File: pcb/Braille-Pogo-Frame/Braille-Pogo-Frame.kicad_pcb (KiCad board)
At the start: 2 copper layers, 99 x 95 mm, 64 parts, among them J1 Conn_01x06, J10 Screw_Terminal_01x02, J2 Conn_01x06, J3 Conn_01x06, J4 Conn_01x06, J9 Conn_01x02, M1 Stepper_Motor_bipolar, M2 Stepper_Motor_bipolar, M3 Stepper_Motor_bipolar, M4 Stepper_Motor_bipolar, SW1 SW_Push, SW2 SW_Push, U1 DRV8847SPWR, U2 DRV8847SPWR, U3 DRV8847SPWR, U4 DRV8847SPWR, U9 RP2040-Zero

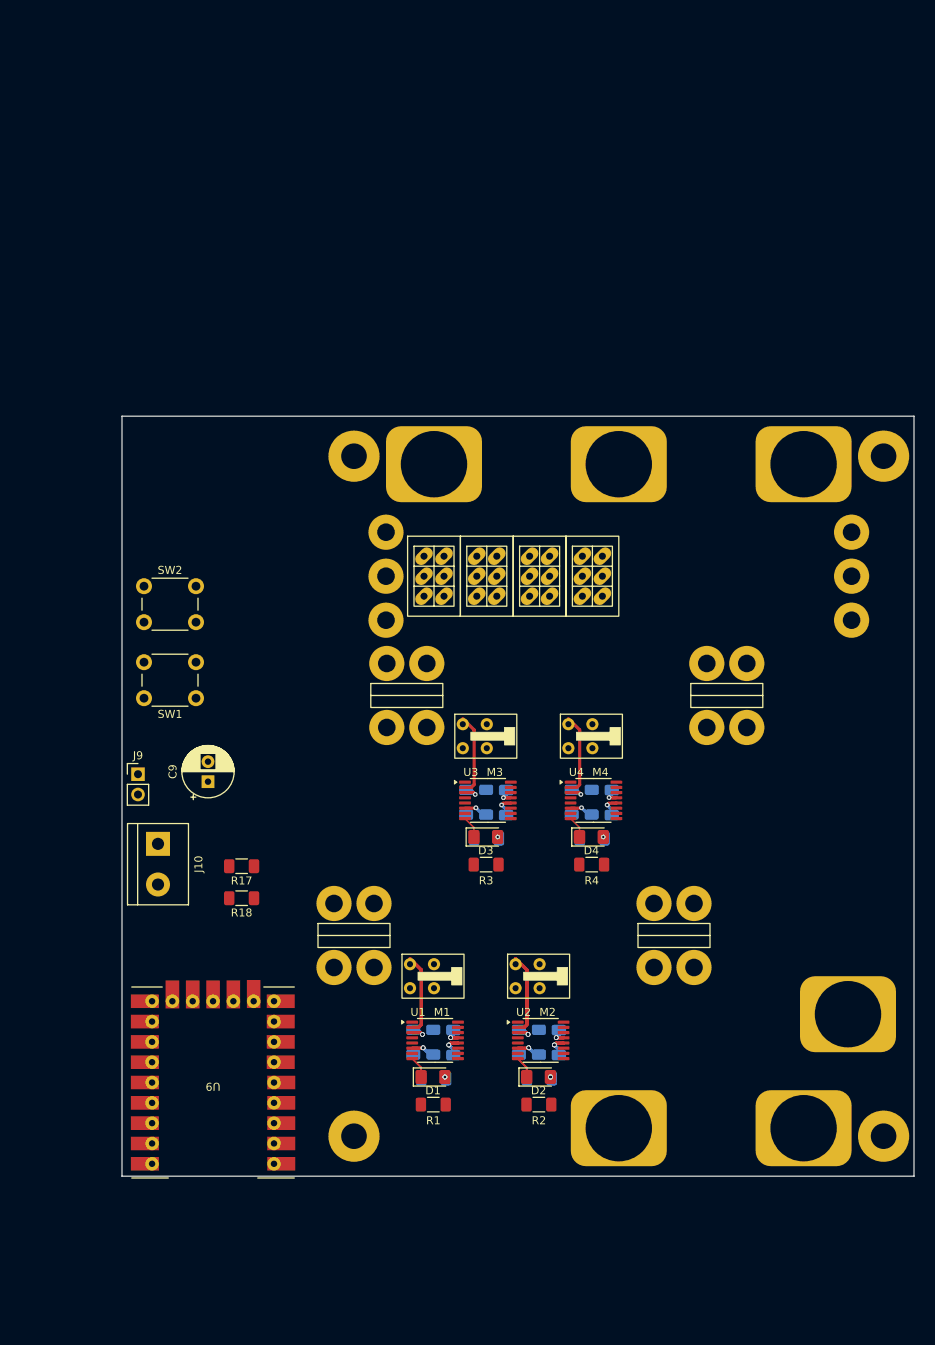
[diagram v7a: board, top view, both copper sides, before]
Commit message: Clean up layout and spacing
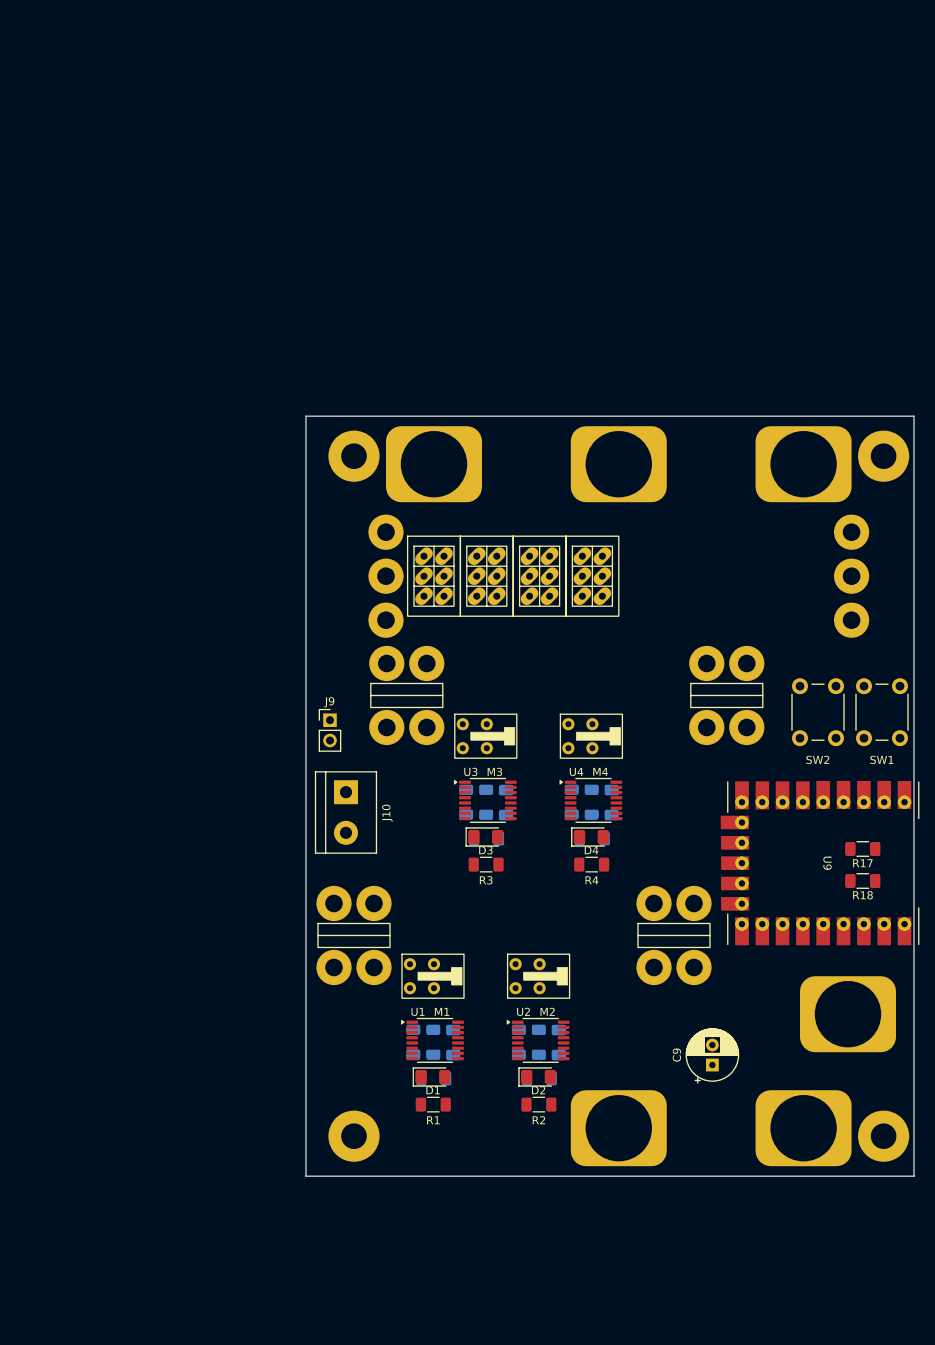
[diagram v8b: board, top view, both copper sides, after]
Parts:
- moved SW1 88.0 mm to (158.2, 113.8), turned to -90 degrees
- moved SW2 87.4 mm to (150.2, 113.8), turned to -90 degrees
- moved R17 77.7 mm to (153.6, 134.1)
- moved R18 77.7 mm to (153.6, 138.1)
- moved C9 72.3 mm to (134.8, 161.1)
- moved U9 58.8 mm to (135.8, 125.7), turned to -90 degrees
- moved J9 24.9 mm to (87.0, 118.0)
- moved J10 24.4 mm to (89.0, 127.0)
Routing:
- net Net-(U2-OUT1): track 20.2 -> 0.00 mm
- net Net-(U1-OUT1): track 20.2 -> 0.00 mm
- net Vdrive: track 16.6 -> 0.00 mm, vias 6 -> 0
- net GND: track 12.1 -> 0.00 mm, vias 6 -> 0
- net Net-(U3-OUT1): track 10.1 -> 0.00 mm
- net Net-(U4-OUT1): track 10.1 -> 0.00 mm
- net Net-(U2-ISEN34): track 6.02 -> 0.00 mm, vias 2 -> 0
- net Net-(U1-ISEN34): track 6.02 -> 0.00 mm, vias 2 -> 0
- net /Braille_Cell1/~{FAULT}: track 5.52 -> 0.00 mm
- net /Braille_Cell/~{FAULT}: track 5.52 -> 0.00 mm
- net Net-(U2-ISEN12): track 5.52 -> 0.00 mm, vias 2 -> 0
- net Net-(U1-ISEN12): track 5.52 -> 0.00 mm, vias 2 -> 0
- net Net-(U4-ISEN34): track 3.01 -> 0.00 mm, vias 1 -> 0
- net Net-(U3-ISEN34): track 3.01 -> 0.00 mm, vias 1 -> 0
- net /Braille_Cell3/~{FAULT}: track 2.76 -> 0.00 mm
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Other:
- board size 99 x 95 mm -> 76 x 95 mm
